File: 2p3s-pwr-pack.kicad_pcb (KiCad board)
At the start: 2 copper layers, 156.8 x 76.8 mm, 21 parts, among them P1 PAD, P10 PAD, P11 PAD, P12 PAD, P13 Conn_Basic_2_pin, P14 PAD, P15 PAD, P2 PAD, P3 PAD, P4 PAD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

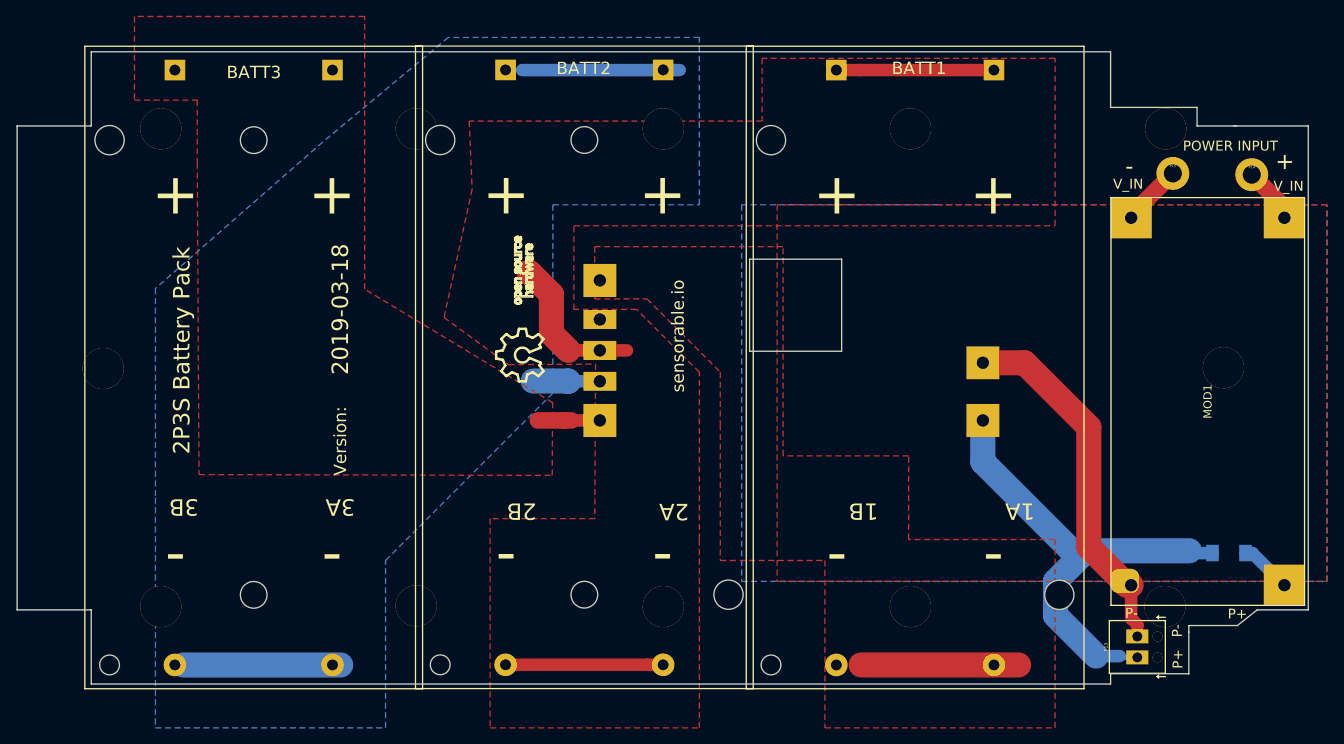
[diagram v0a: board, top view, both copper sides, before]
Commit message: Finish JIRA EL-169 changes
move battery holders, change some holes, add current sensing diode, updates to logo, VIN terminal block
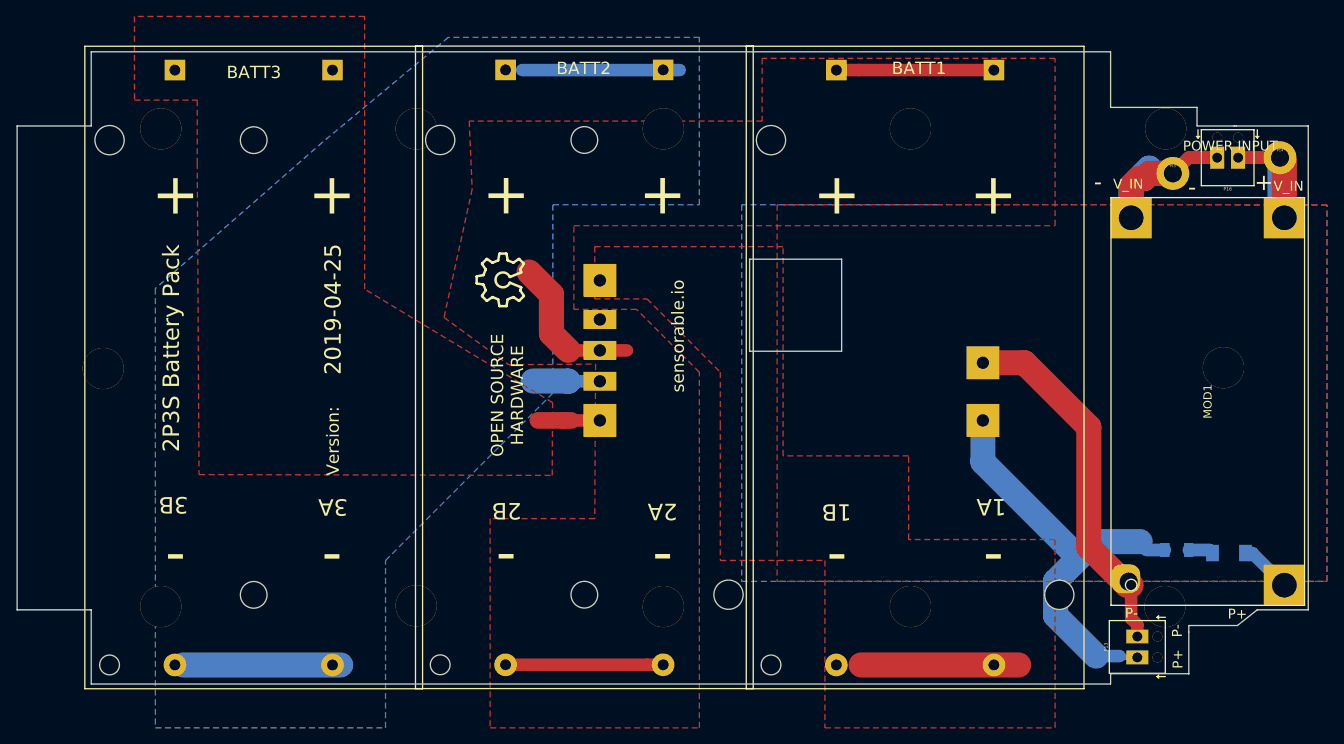
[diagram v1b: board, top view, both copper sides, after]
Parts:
- added P16: Conn_Basic_2_pin, Footprints:TERM_BLK_2_SIDE_2.54MM, F.Cu at (196.2, 78.1)
- added R1: 0.01, Footprints:1206_Medium_Pads, B.Cu at (190.0, 125.7)
- moved P14 4.00 mm to (202.6, 78.1)
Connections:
- net Net-(MOD1-Pad2) renamed V_IN-
- net V_IN renamed V_IN+
- D1 pad 1: P+ -> Net-(D1-Pad1)
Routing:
- net V_IN-: track 7.49 -> 32.3 mm
- net V_IN+: track 6.88 -> 25.2 mm
- net P+: track 58.9 -> 52.9 mm
- net Net-(D1-Pad1): track 0.00 -> 3.04 mm
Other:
- board text added: "2019-04-25"
- board text added: "OPEN SOURCE HARDWARE"

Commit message: remove hole in the way
battery mounting clip in the middle interfered with enclosure stantion boss. removed the battery mounting clip
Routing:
- net P+: track 52.9 -> 66.8 mm
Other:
- board text added: "2019-04-30"
- board text removed: "2019-03-18"
- board text removed: "2019-04-25"
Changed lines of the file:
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@@
     (thickness 1.6)
     (drawings 258)
-    (tracks 66)
+    (tracks 68)
     (zones 0)
     (modules 23)
@@
     (mod_text_size 1 1)
     (mod_text_width 0.15)
-    (pad_size 2.2 1.6)
-    (pad_drill 1)
+    (pad_size 0.1524 0.1524)
+    (pad_drill 0)
     (pad_to_mask_clearance 0)
     (solder_mask_min_width 0.1016)
@@
       (drillshape 0)
       (scaleselection 1)
-      (outputdirectory "Gerbers3Mar2019"))
+      (outputdirectory "Gerbers27apr2019"))
   )
   (net 0 "")
@@
     (pad "" np_thru_hole circle (at -17.5 36.11) (size 2.4 2.4) (drill 2.4) (layers *.Cu *.Mask))
     (pad "" np_thru_hole circle (at 17.5 27.6) (size 3.55 3.55) (drill 3.55) (layers *.Cu *.Mask))
-    (pad "" np_thru_hole circle (at -17.5 -27.6) (size 3.55 3.55) (drill 3.55) (layers *.Cu *.Mask))
+    (pad "" smd circle (at -17.5 -27.6) (size 0.1524 0.1524) (layers F.Cu F.Paste F.Mask))
     (pad "" np_thru_hole circle (at 0 27.6) (size 3.24 3.24) (drill 3.24) (layers *.Cu *.Mask))
     (pad "" np_thru_hole circle (at 0 -27.6) (size 3.24 3.24) (drill 3.24) (layers *.Cu *.Mask))
@@
     (effects (font (size 1.5 1.5) (thickness 0.3)) (justify mirror))
   )
-  (gr_text 2019-03-18 (at 72.4208 87.992) (layer B.SilkS)
+  (gr_text 2019-04-30 (at 72.4208 87.992) (layer B.SilkS)
     (effects (font (size 2 2) (thickness 0.3)) (justify mirror))
   )
@@
     (effects (font (size 1.2 1.2) (thickness 0.3)) (justify mirror))
   )
-  (gr_text P- (at 184.4548 126.111) (layer B.SilkS)
+  (gr_text P- (at 183.388 126.3777) (layer B.SilkS)
     (effects (font (size 1.2 1.2) (thickness 0.3)) (justify mirror))
   )
-  (gr_text "GND\n" (at 183.5404 126.0475) (layer B.SilkS)
+  (gr_text "GND\n" (at 180.6194 129.0447 90) (layer B.SilkS)
     (effects (font (size 1.2 1.2) (thickness 0.3)) (justify mirror))
   )
@@
     (effects (font (size 1.2 1.2) (thickness 0.3)))
   )
-  (gr_text 2019-04-25 (at 87.611 96.5 90) (layer F.SilkS)
+  (gr_text 2019-04-30 (at 87.611 96.5 90) (layer F.SilkS)
     (effects (font (size 2 2) (thickness 0.3)))
   )
@@
   (segment (start 185.25 138.77) (end 183.265 138.77) (width 0.635) (layer B.Cu) (net 5))
   (segment (start 183.1028 138.6078) (end 180.2384 138.6078) (width 1.524) (layer B.Cu) (net 5))
-  (segment (start 175.3236 129.518328) (end 179.018329 125.823599) (width 3.048) (layer B.Cu) (net 5))
-  (segment (start 180.2384 138.6078) (end 175.3236 133.693) (width 3.048) (layer B.Cu) (net 5))
-  (segment (start 175.3236 133.693) (end 175.3236 129.518328) (width 3.048) (layer B.Cu) (net 5))
   (segment (start 177.275599 125.823599) (end 179.018329 125.823599) (width 3.048) (layer B.Cu) (net 5))
   (segment (start 166.5 110) (end 166.5 115.048) (width 3.048) (layer B.Cu) (net 5))
-  (segment (start 166.5 115.048) (end 177.275599 125.823599) (width 3.048) (layer B.Cu) (net 5))
   (segment (start 186.3344 125.73) (end 188.595 125.73) (width 1.524) (layer B.Cu) (net 5))
   (segment (start 179.018329 125.823599) (end 179.111928 125.73) (width 3.048) (layer B.Cu) (net 5))
@@
   (segment (start 179.560601 125.823599) (end 180.6702 124.714) (width 3.048) (layer B.Cu) (net 5))
   (segment (start 180.6702 124.714) (end 185.5978 124.714) (width 3.048) (layer B.Cu) (net 5))
+  (segment (start 177.7873 138.6078) (end 173.736 138.6078) (width 3.048) (layer B.Cu) (net 5))
+  (segment (start 177.7873 138.6078) (end 180.2384 138.6078) (width 3.048) (layer B.Cu) (net 5))
+  (segment (start 168.5036 133.3754) (end 168.5036 117.0516) (width 3.048) (layer B.Cu) (net 5))
+  (segment (start 173.736 138.6078) (end 168.5036 133.3754) (width 3.048) (layer B.Cu) (net 5))
+  (segment (start 166.5 115.048) (end 168.5036 117.0516) (width 3.048) (layer B.Cu) (net 5))
+  (segment (start 168.5036 117.0516) (end 177.275599 125.823599) (width 3.048) (layer B.Cu) (net 5))
   (segment (start 129.690001 67.465001) (end 110.560001 67.465001) (width 1.524) (layer B.Cu) (net 6))
   (segment (start 69.410001 139.685001) (end 88.540001 139.685001) (width 3.048) (layer B.Cu) (net 6))

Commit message: KiCAD design files as in 3May2019 gerber files
These are the KICAD design files that the may3 gerber outputs were produced from.
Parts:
- added P17: PAD, NPTH_3mm, F.Cu at (53.3, 124.2)
- added P19: PAD, NPTH_3mm, F.Cu at (53.3, 82.0)
- moved P15 0.51 mm to (189.6, 80.5)
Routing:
- net V_IN-: track 32.3 -> 21.6 mm
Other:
- board text added: "2019-05-04"
- board text removed: "2019-04-30"
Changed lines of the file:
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@@
     (thickness 1.6)
     (drawings 258)
-    (tracks 68)
+    (tracks 61)
     (zones 0)
-    (modules 23)
+    (modules 25)
     (nets 12)
   )
@@
   )
   (setup
-    (last_trace_width 3.048)
+    (last_trace_width 0.1524)
     (user_trace_width 0.1524)
     (user_trace_width 0.254)
@@
       (drillshape 0)
       (scaleselection 1)
-      (outputdirectory "Gerbers27apr2019"))
+      (outputdirectory "Gerbers3May2019"))
   )
   (net 0 "")
@@
   )
   (module Footprints:HOLE_4mmx2.2mm (layer F.Cu)
-    (at 189.5602 80.01)
+    (at 189.5602 80.518)
     (fp_text reference P15 (at 0 -0.9) (layer F.SilkS)
       (effects (font (size 0.3 0.3) (thickness 0.075)))
@@
     )
   )
+  (module NPTH_3mm (layer F.Cu)
+    (at 53.34 124.206)
+    (fp_text reference P17 (at 0 0) (layer F.SilkS) hide
+      (effects (font (size 0.127 0.127) (thickness 0.03175)))
+    )
+    (fp_text value PAD (at 0 0) (layer F.Fab) hide
+      (effects (font (size 0.127 0.127) (thickness 0.03175)))
+    )
+    (pad "" np_thru_hole circle (at 0 0) (size 3 3) (drill 3) (layers *.Cu *.Mask)
+      (clearance 1))
+  )
+  (module NPTH_3mm (layer F.Cu)
+    (at 53.34 82.042)
+    (fp_text reference P19 (at 0 0) (layer F.SilkS) hide
+      (effects (font (size 0.127 0.127) (thickness 0.03175)))
+    )
+    (fp_text value PAD (at 0 0) (layer F.Fab) hide
+      (effects (font (size 0.127 0.127) (thickness 0.03175)))
+    )
+    (pad "" np_thru_hole circle (at 0 0) (size 3 3) (drill 3) (layers *.Cu *.Mask)
+      (clearance 1))
+  )
   (gr_text "OPEN SOURCE\nHARDWARE" (at 108.7755 106.9467 90) (layer F.SilkS)
     (effects (font (size 1.5 1.5) (thickness 0.3)))
@@
     (effects (font (size 2 2) (thickness 0.3)) (justify mirror))
   )
-  (gr_text "DO NOT TIE\nTO GND" (at 184.1627 77.6224) (layer B.SilkS)
+  (gr_text "DO NOT TIE\nTO GND" (at 184.404 78.74) (layer B.SilkS)
     (effects (font (size 0.6 0.6) (thickness 0.15)) (justify mirror))
   )
@@
     (effects (font (size 1.5 1.5) (thickness 0.3)) (justify mirror))
   )
-  (gr_text 2019-04-30 (at 72.4208 87.992) (layer B.SilkS)
+  (gr_text 2019-05-04 (at 72.4208 87.992) (layer B.SilkS)
     (effects (font (size 2 2) (thickness 0.3)) (justify mirror))
   )
@@
     (effects (font (size 1.2 1.2) (thickness 0.3)))
   )
-  (gr_text 2019-04-30 (at 87.611 96.5 90) (layer F.SilkS)
+  (gr_text 2019-05-04 (at 87.611 96.5 90) (layer F.SilkS)
     (effects (font (size 2 2) (thickness 0.3)))
   )
@@
   (segment (start 191.4652 78.105) (end 189.5602 80.01) (width 1.524) (layer F.Cu) (net 10))
   (segment (start 194.945 78.105) (end 191.4652 78.105) (width 1.524) (layer F.Cu) (net 10))
-  (segment (start 186.731773 80.01) (end 186.096773 80.645) (width 3.048) (layer F.Cu) (net 10))
-  (segment (start 189.5602 80.01) (end 186.731773 80.01) (width 3.048) (layer F.Cu) (net 10))
-  (segment (start 186.096773 80.645) (end 185.42 80.645) (width 3.048) (layer F.Cu) (net 10))
-  (segment (start 184.5 81.565) (end 184.5 85.4) (width 3.048) (layer F.Cu) (net 10))
-  (segment (start 185.42 80.645) (end 184.5 81.565) (width 3.048) (layer F.Cu) (net 10))
-  (segment (start 184.5 85.4) (end 184.5 81.565) (width 3.048) (layer B.Cu) (net 10))
-  (segment (start 184.5 81.565) (end 186.69 79.375) (width 3.048) (layer B.Cu) (net 10))
-  (segment (start 186.731773 80.01) (end 189.5602 80.01) (width 3.048) (layer B.Cu) (net 10))
-  (segment (start 186.69 79.375) (end 186.69 79.968227) (width 3.048) (layer B.Cu) (net 10))
-  (segment (start 186.69 79.968227) (end 186.731773 80.01) (width 3.048) (layer B.Cu) (net 10))
   (segment (start 191.4652 78.105) (end 189.5602 80.01) (width 1.524) (layer B.Cu) (net 10))
   (segment (start 194.945 78.105) (end 191.4652 78.105) (width 1.524) (layer B.Cu) (net 10))
+  (segment (start 184.5 85.4) (end 184.5 81.692) (width 3.048) (layer B.Cu) (net 10))
+  (segment (start 185.674 80.518) (end 189.5602 80.518) (width 3.048) (layer B.Cu) (net 10))
+  (segment (start 184.5 81.692) (end 185.674 80.518) (width 3.048) (layer B.Cu) (net 10))
   (segment (start 194.0118 125.73) (end 194.3801 126.0983) (width 1.524) (layer B.Cu) (net 11))
   (segment (start 191.495 125.73) (end 194.0118 125.73) (width 1.524) (layer B.Cu) (net 11))
@@
     (connect_pads (clearance 1.5))
     (min_thickness 0.254)
-    (fill yes (arc_segments 16) (thermal_gap 0.762) (thermal_bridge_width 0.635))
+    (fill yes (arc_segments 16) (thermal_gap 0.762) (thermal_bridge_width 0.635) (smoothing fillet) (radius 3.81))
     (polygon
       (pts
@@
     (connect_pads (clearance 1.5))
     (min_thickness 0.254)
-    (fill yes (arc_segments 16) (thermal_gap 0.762) (thermal_bridge_width 0.635))
+    (fill yes (arc_segments 16) (thermal_gap 0.762) (thermal_bridge_width 0.635) (smoothing fillet) (radius 3.81))
     (polygon
       (pts
@@
     (connect_pads (clearance 1.5))
     (min_thickness 0.254)
-    (fill yes (arc_segments 16) (thermal_gap 0.762) (thermal_bridge_width 0.635))
+    (fill yes (arc_segments 16) (thermal_gap 0.762) (thermal_bridge_width 0.635) (smoothing fillet) (radius 3.81))
     (polygon
       (pts
@@
     (connect_pads (clearance 1.5))
     (min_thickness 0.254)
-    (fill yes (arc_segments 16) (thermal_gap 0.762) (thermal_bridge_width 0.635))
+    (fill yes (arc_segments 16) (thermal_gap 0.762) (thermal_bridge_width 0.635) (smoothing fillet) (radius 3.81))
     (polygon
       (pts
@@
     (connect_pads (clearance 1.5))
     (min_thickness 0.254)
-    (fill yes (arc_segments 16) (thermal_gap 0.762) (thermal_bridge_width 0.635))
+    (fill yes (arc_segments 16) (thermal_gap 0.762) (thermal_bridge_width 0.635) (smoothing fillet) (radius 3.81))
     (polygon
       (pts
@@
     (connect_pads (clearance 1.5))
     (min_thickness 0.254)
-    (fill yes (arc_segments 16) (thermal_gap 0.762) (thermal_bridge_width 0.635))
+    (fill yes (arc_segments 16) (thermal_gap 0.762) (thermal_bridge_width 0.635) (smoothing fillet) (radius 3.81))
     (polygon
       (pts
